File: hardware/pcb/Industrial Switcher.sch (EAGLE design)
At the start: 45 parts, among them IC1 MSP430FR5739, IC2 HY-TFT220, Q1 IRFR5305, Q2 32 kHz, Q3 IRFZ34NS, Q4 IRFZ34NS, Q5 IRFZ34NS, Q6 IRFZ34NS, U1 TDA3664, U2 TPS76933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

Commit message: Routing almost finished.
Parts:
- added C14: 68uF, rcl:CPOL-EUF
- added H1, H2, H3, H4: MOUNT-HOLE3.0, holes:MOUNT-HOLE3.0
- added POWER: (no value), SparkFun:M025MM
- C13: device rcl:C-EUC0603 -> rcl:C-EUC0805
- C6: value 100uF -> 68uF; device rcl:CPOL-EUG -> rcl:CPOL-EUF
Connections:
- removed net N$1: D1.C, Q1.S, U1.VP
- removed net N$16: R9.1, U3.SENSE2
- removed net N$17: R8.1, U3.SENSE1
- new net N$23: Q5.G, U3.GATE2
- new net N$24: Q4.G, U3.GATE3
- new net N$25: Q3.G, U3.GATE4
- net +24V: now also C14.+, D1.C, Q1.S, U1.VP; no longer Q1.D
- net GND: now also C14.-, POWER.2
- net N$10: now also R11.1, U3.SENSE1; no longer Q4.G, U3.GATE2
- net N$13: now also POWER.1, Q1.D; no longer Q3.G, U3.GATE1
- net N$18: now also Q6.G, U3.GATE1; no longer R10.1, U3.SENSE3
- net N$4: now also R8.1; no longer R11.1
- net N$5: now also R9.1, U3.SENSE3; no longer Q6.G, U3.GATE4
- net N$7: now also R10.1, U3.SENSE2; no longer Q5.G, U3.GATE3
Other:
- note added: "Input 12 to 30V, maybe even more"
- moved on the sheet: C1, C4, C5, C6, LOAD1, LOAD2, LOAD3, LOAD4, Q1, Q3, Q4, Q5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

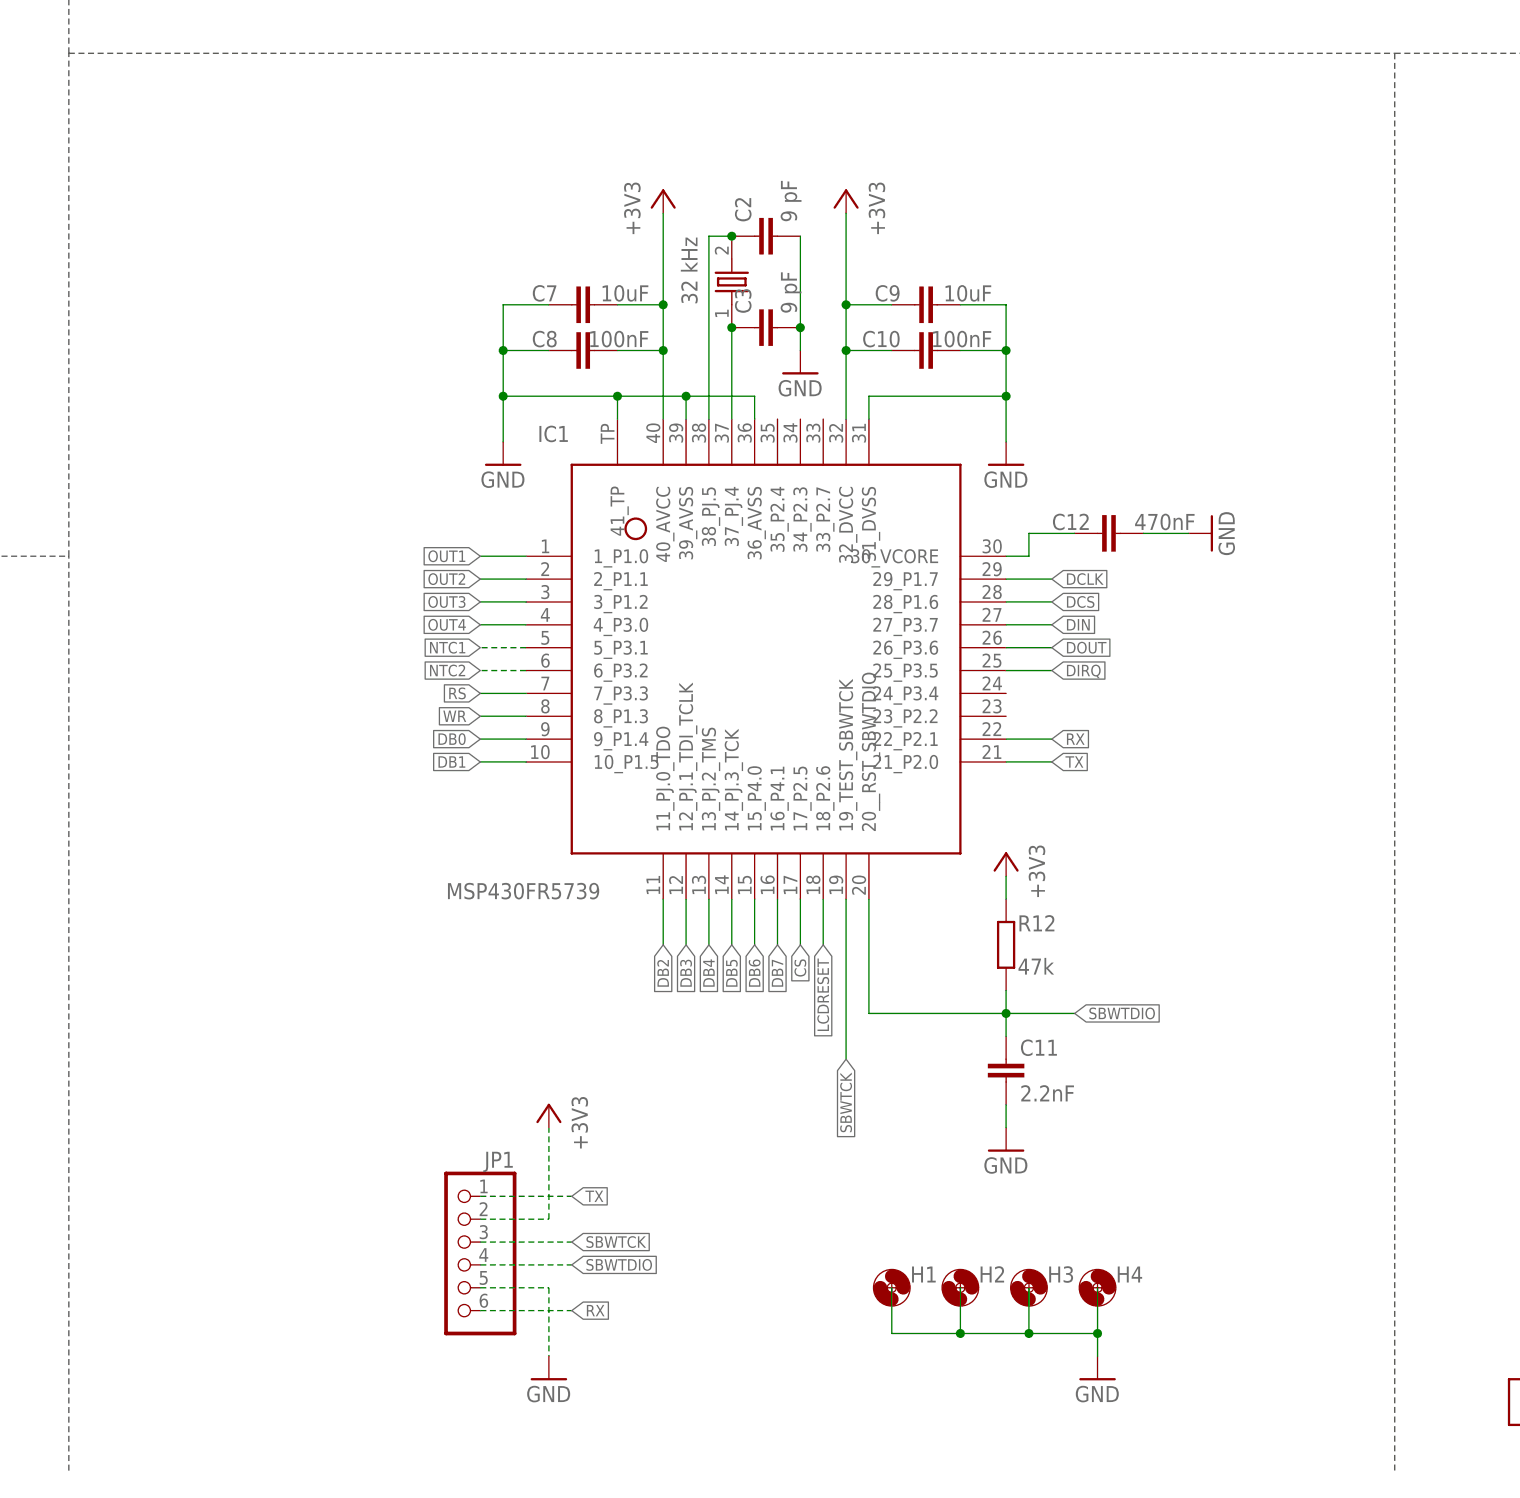
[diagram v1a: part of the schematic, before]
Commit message: Rearranged pins for better layout.
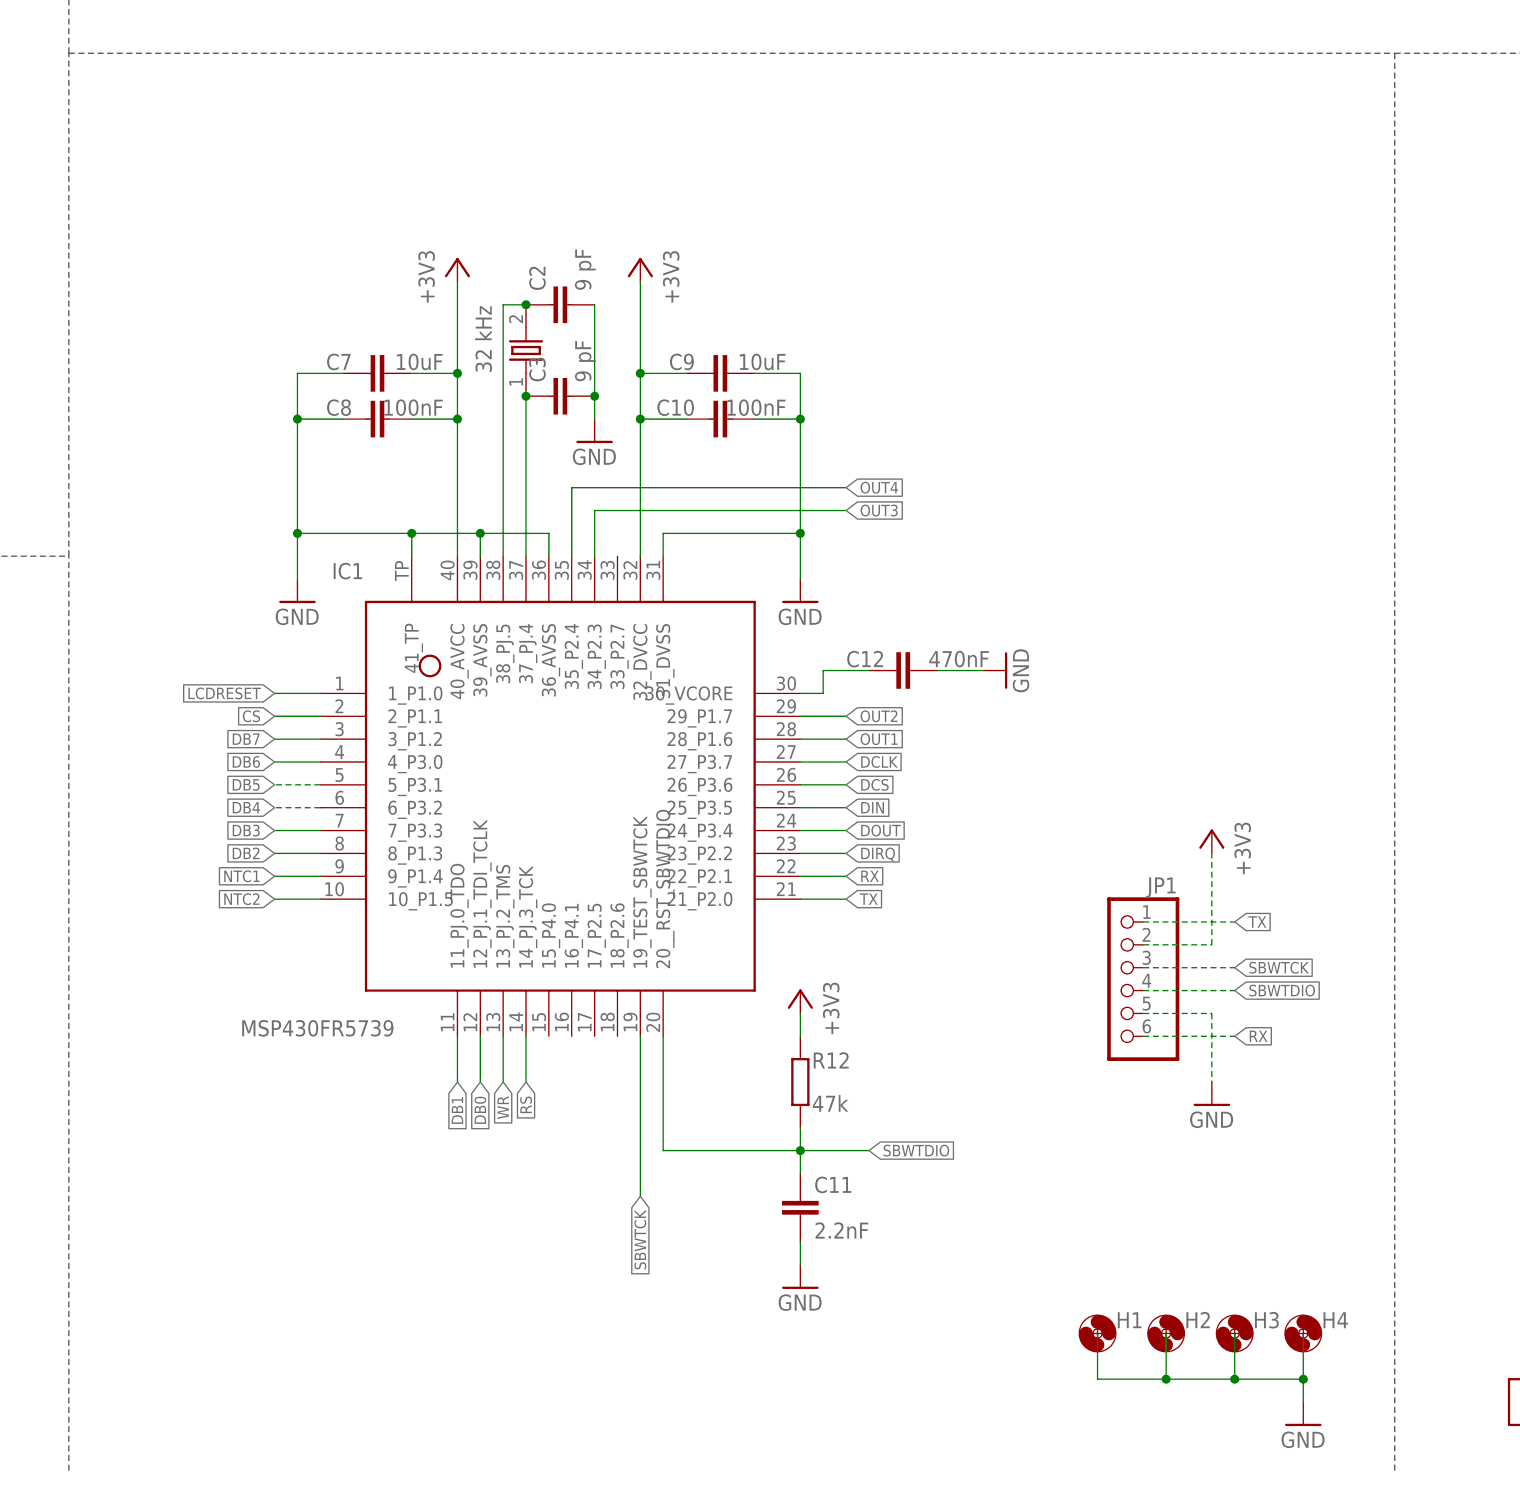
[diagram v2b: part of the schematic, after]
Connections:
- net CS: now also IC1.2_P1.1; no longer IC1.17_P2.5
- net DB0: now also IC1.12_PJ.1_TDI_TCLK; no longer IC1.9_P1.4
- net DB1: now also IC1.11_PJ.0_TDO; no longer IC1.10_P1.5
- net DB2: now also IC1.8_P1.3; no longer IC1.11_PJ.0_TDO
- net DB3: now also IC1.7_P3.3; no longer IC1.12_PJ.1_TDI_TCLK
- net DB4: now also IC1.6_P3.2; no longer IC1.13_PJ.2_TMS
- net DB5: now also IC1.5_P3.1; no longer IC1.14_PJ.3_TCK
- net DB6: now also IC1.4_P3.0; no longer IC1.15_P4.0
- net DB7: now also IC1.3_P1.2; no longer IC1.16_P4.1
- net DCLK: now also IC1.27_P3.7; no longer IC1.29_P1.7
- net DCS: now also IC1.26_P3.6; no longer IC1.28_P1.6
- net DIN: now also IC1.25_P3.5; no longer IC1.27_P3.7
- net DIRQ: now also IC1.23_P2.2; no longer IC1.25_P3.5
- net DOUT: now also IC1.24_P3.4; no longer IC1.26_P3.6
- net LCDRESET: now also IC1.1_P1.0; no longer IC1.18_P2.6
- net NTC1: now also IC1.9_P1.4; no longer IC1.5_P3.1
- net NTC2: now also IC1.10_P1.5; no longer IC1.6_P3.2
- net OUT1: now also IC1.28_P1.6; no longer IC1.1_P1.0
- net OUT2: now also IC1.29_P1.7; no longer IC1.2_P1.1
- net OUT3: now also IC1.34_P2.3; no longer IC1.3_P1.2
- net OUT4: now also IC1.35_P2.4; no longer IC1.4_P3.0
- net RS: now also IC1.14_PJ.3_TCK; no longer IC1.7_P3.3
- net WR: now also IC1.13_PJ.2_TMS; no longer IC1.8_P1.3
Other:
- moved on the sheet: C10, C11, C12, C2, C3, C7, C8, C9, H1, H2, H3, H4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

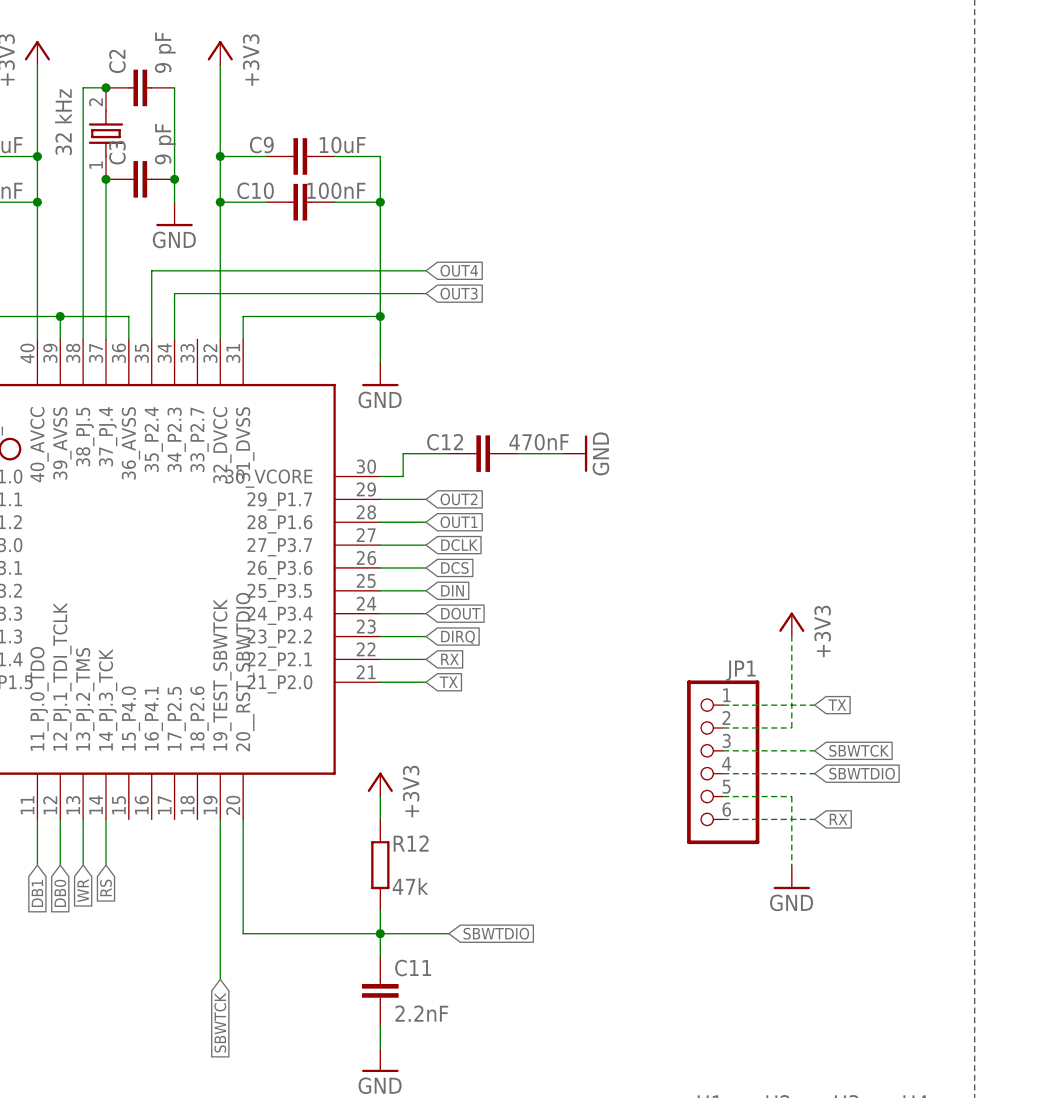
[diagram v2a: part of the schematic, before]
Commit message: Added LEDs and did some more routing.
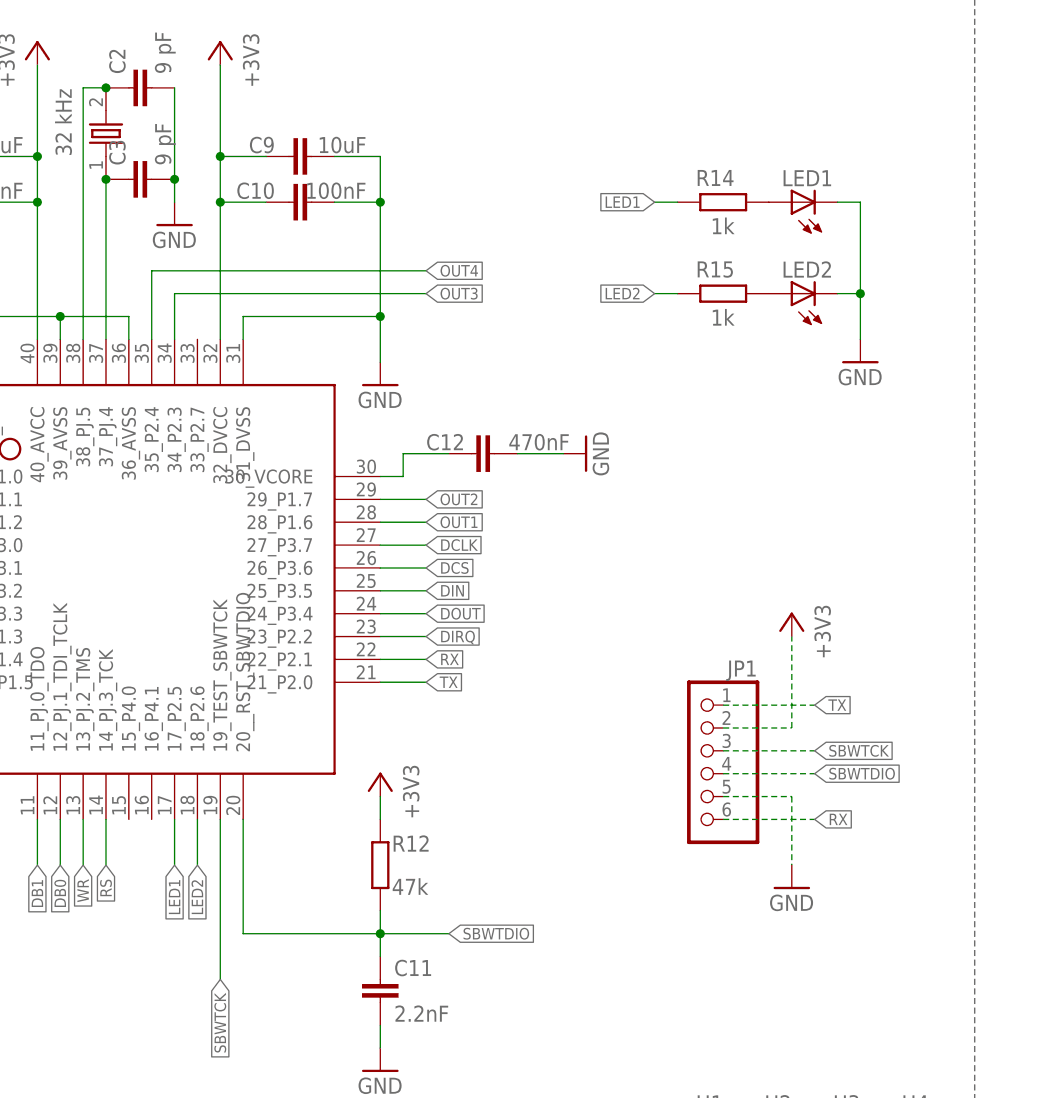
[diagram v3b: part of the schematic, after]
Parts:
- added LED1, LED2: (no value), led:LEDCHIP-LED0603
- added R14, R15: 1k, rcl:R-EU_R0402
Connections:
- new net LED1: IC1.17_P2.5, R14.2
- new net LED2: IC1.18_P2.6, R15.2
- new net N$26: LED1.A, R14.1
- new net N$27: LED2.A, R15.1
- net GND: now also LED1.C, LED2.C
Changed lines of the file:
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@@
 <part name="GND20" library="supply1" deviceset="GND" device=""/>
 <part name="GND21" library="supply1" deviceset="GND" device=""/>
+<part name="LED1" library="led" deviceset="LED" device="CHIP-LED0603"/>
+<part name="LED2" library="led" deviceset="LED" device="CHIP-LED0603"/>
+<part name="GND22" library="supply1" deviceset="GND" device=""/>
+<part name="R14" library="rcl" deviceset="R-EU_" device="R0402" value="1k"/>
+<part name="R15" library="rcl" deviceset="R-EU_" device="R0402" value="1k"/>
 </parts>
 <sheets>
@@
 <instance part="GND20" gate="1" x="238.76" y="233.68" rot="R90"/>
 <instance part="GND21" gate="1" x="200.66" y="233.68" rot="R270"/>
+<instance part="LED1" gate="G$1" x="238.76" y="121.92" rot="R90"/>
+<instance part="LED2" gate="G$1" x="238.76" y="111.76" rot="R90"/>
+<instance part="GND22" gate="1" x="246.38" y="104.14"/>
+<instance part="R14" gate="G$1" x="231.14" y="121.92" smashed="yes" rot="R180">
+<attribute name="NAME" x="232.41" y="125.5014" size="1.778" layer="95" rot="R180"/>
+<attribute name="VALUE" x="232.41" y="120.142" size="1.778" layer="96" rot="R180"/>
+</instance>
+<instance part="R15" gate="G$1" x="231.14" y="111.76" smashed="yes" rot="R180">
+<attribute name="NAME" x="232.41" y="115.3414" size="1.778" layer="95" rot="R180"/>
+<attribute name="VALUE" x="232.41" y="109.982" size="1.778" layer="96" rot="R180"/>
+</instance>
 </instances>
 <busses>
@@
 <pinref part="GND20" gate="1" pin="GND"/>
 <wire x1="233.68" y1="233.68" x2="236.22" y2="233.68" width="0.1524" layer="91"/>
+</segment>
+<segment>
+<pinref part="LED2" gate="G$1" pin="C"/>
+<wire x1="243.84" y1="111.76" x2="246.38" y2="111.76" width="0.1524" layer="91"/>
+<pinref part="GND22" gate="1" pin="GND"/>
+<wire x1="246.38" y1="111.76" x2="246.38" y2="106.68" width="0.1524" layer="91"/>
+<pinref part="LED1" gate="G$1" pin="C"/>
+<wire x1="243.84" y1="121.92" x2="246.38" y2="121.92" width="0.1524" layer="91"/>
+<wire x1="246.38" y1="121.92" x2="246.38" y2="111.76" width="0.1524" layer="91"/>
+<junction x="246.38" y="111.76"/>
 </segment>
 </net>
@@
 </segment>
 </net>
+<net name="N$26" class="0">
+<segment>
+<pinref part="LED1" gate="G$1" pin="A"/>
+<pinref part="R14" gate="G$1" pin="1"/>
+</segment>
+</net>
+<net name="N$27" class="0">
+<segment>
+<pinref part="LED2" gate="G$1" pin="A"/>
+<pinref part="R15" gate="G$1" pin="1"/>
+</segment>
+</net>
+<net name="LED2" class="0">
+<segment>
+<pinref part="R15" gate="G$1" pin="2"/>
+<wire x1="226.06" y1="111.76" x2="223.52" y2="111.76" width="0.1524" layer="91"/>
+<label x="223.52" y="111.76" size="1.27" layer="95" rot="R180" xref="yes"/>
+</segment>
+<segment>
+<pinref part="IC1" gate="G$1" pin="18_P2.6"/>
+<wire x1="172.72" y1="53.34" x2="172.72" y2="48.26" width="0.1524" layer="91"/>
+<label x="172.72" y="48.26" size="1.27" layer="95" rot="R270" xref="yes"/>
+</segment>
+</net>
+<net name="LED1" class="0">
+<segment>
+<pinref part="R14" gate="G$1" pin="2"/>
+<wire x1="226.06" y1="121.92" x2="223.52" y2="121.92" width="0.1524" layer="91"/>
+<label x="223.52" y="121.92" size="1.27" layer="95" rot="R180" xref="yes"/>
+</segment>
+<segment>
+<pinref part="IC1" gate="G$1" pin="17_P2.5"/>
+<wire x1="170.18" y1="53.34" x2="170.18" y2="48.26" width="0.1524" layer="91"/>
+<label x="170.18" y="48.26" size="1.27" layer="95" rot="R270" xref="yes"/>
+</segment>
+</net>

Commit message: Added optional flyback diodes to loads.
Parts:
- added D2, D3, D4, D5: 1N4148WS, diode:DIODE-SOD323-W
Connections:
- net GND: now also D2.A, D3.A, D4.A, D5.A
- net N$12: now also D4.C
- net N$15: now also D5.C
- net N$6: now also D3.C
- net N$9: now also D2.C
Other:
- note added: "Diodes are optinoal. LT1161 already handles inductive loads cleverly."
- note removed: "Notice that there are no diodes for inductive loads. LT1161 handles it cleverly."
- moved on the sheet: C1, C10, C11, C12, C2, C3, C4, C5, C7, C8, C9, H1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
